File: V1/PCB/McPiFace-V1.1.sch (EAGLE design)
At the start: 10 parts, among them J1 MC_PI_FACE_CONNECTORS_LEDSSIDE

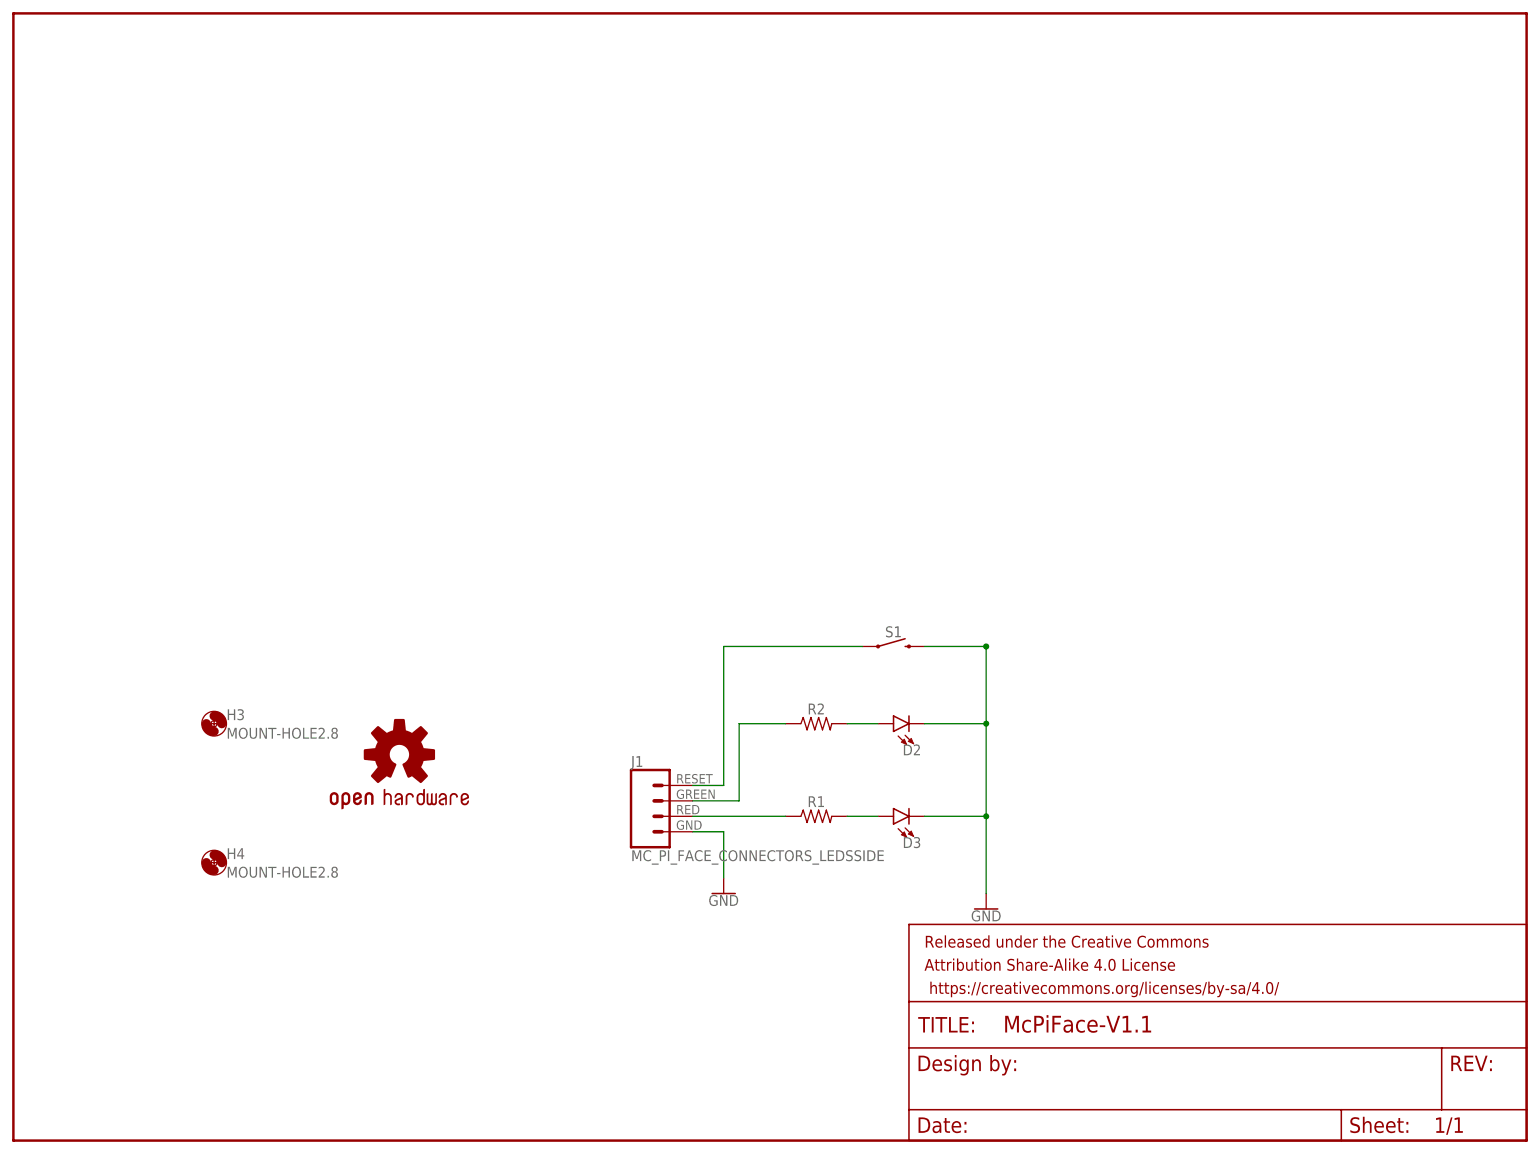
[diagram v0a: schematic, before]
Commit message: Adding V1.1 PCB.
Uses common layout for LEDs, removed vent hole.
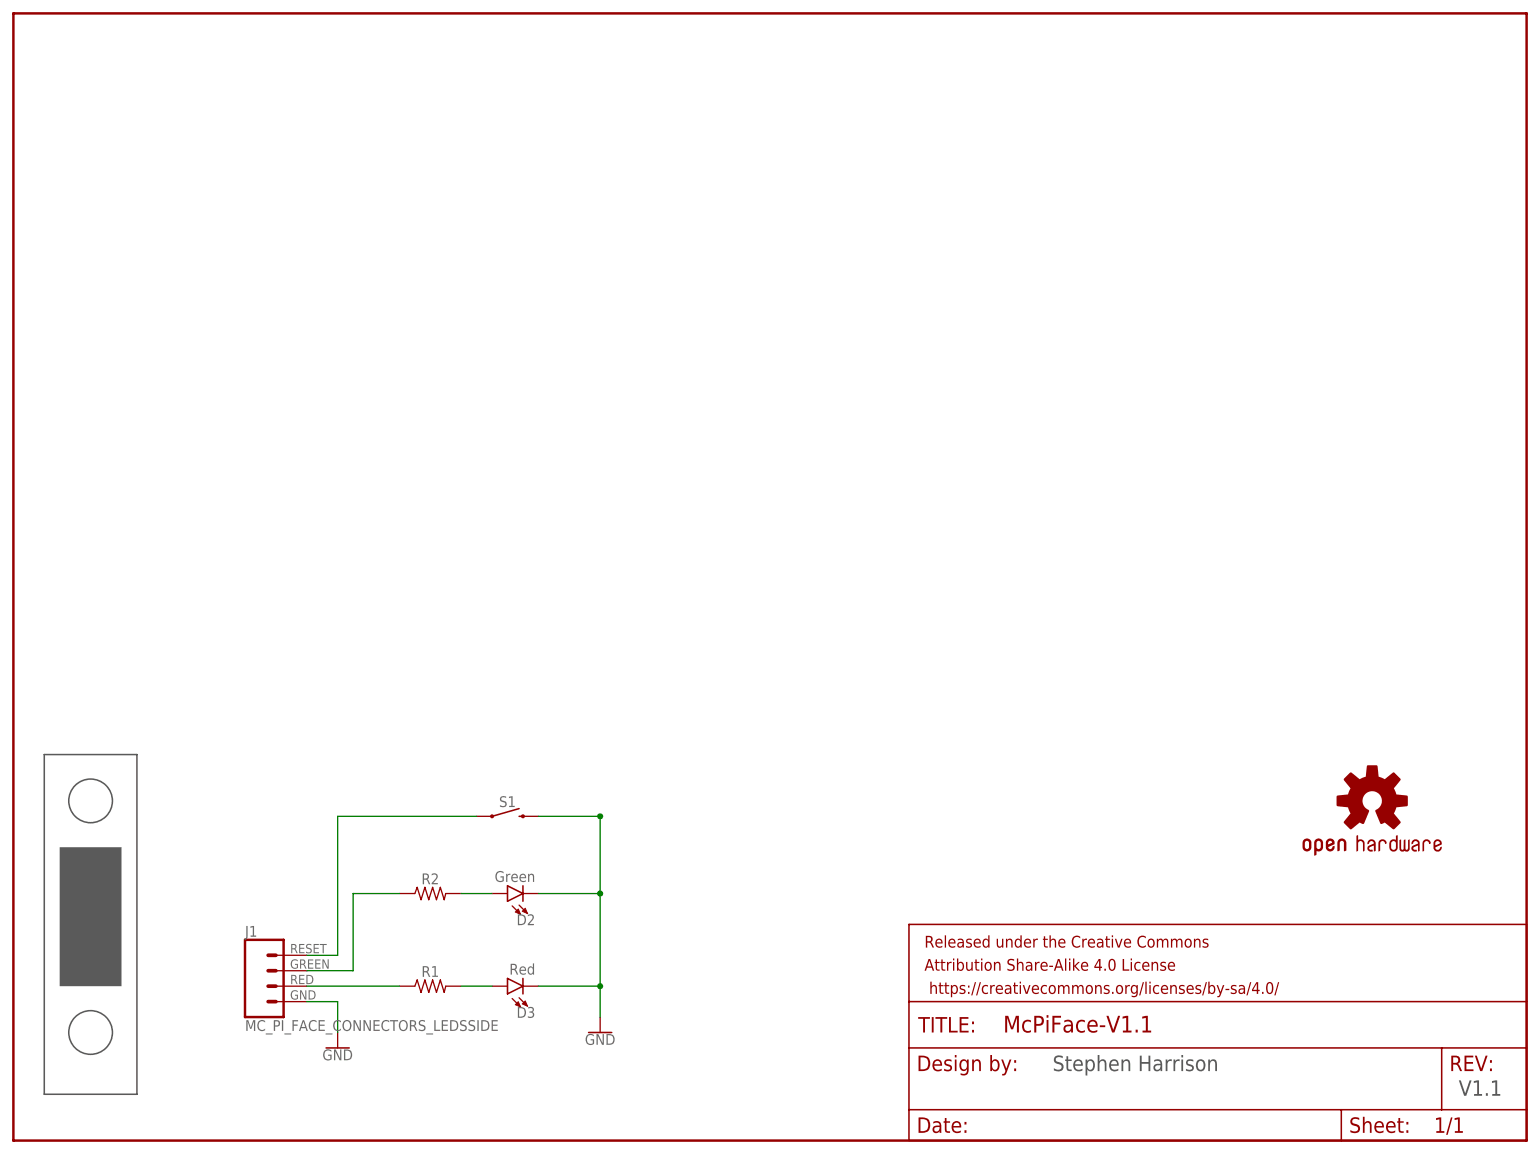
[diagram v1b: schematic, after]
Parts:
- removed H3, H4: MOUNT-HOLE2.8, holes:MOUNT-HOLE2.8
- added U$1: MC_PI_FACE_PANELSINGLE, McPiFace:MC_PI_FACE_PANELSINGLE
- D2: value (none) -> Green
- D3: value (none) -> Red
- R1, R2: device SparkFun-Resistors:RESISTOR1206 -> SparkFun-Resistors:RESISTOR0805
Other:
- note added: "Stephen Harrison"
- note added: "V1.1"
- moved on the sheet: D2, D3, J1, R1, R2, S1
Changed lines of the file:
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@@
 <parts>
 <part name="LOGO1" library="SparkFun-Aesthetics" deviceset="OSHW-LOGO" device="L"/>
-<part name="H3" library="holes" deviceset="MOUNT-HOLE" device="2.8"/>
-<part name="H4" library="holes" deviceset="MOUNT-HOLE" device="2.8"/>
-<part name="D2" library="ThingySticks" deviceset="LED" device="LED-1206-BOTTOM-2.0MM-GREEN"/>
-<part name="D3" library="ThingySticks" deviceset="LED" device="LED-1206-BOTTOM-2.0MM-RED"/>
-<part name="R1" library="SparkFun-Resistors" deviceset="RESISTOR" device="1206" value=" "/>
-<part name="R2" library="SparkFun-Resistors" deviceset="RESISTOR" device="1206" value=" "/>
+<part name="D2" library="ThingySticks" deviceset="LED" device="LED-1206-BOTTOM-2.0MM-GREEN" value="Green"/>
+<part name="D3" library="ThingySticks" deviceset="LED" device="LED-1206-BOTTOM-2.0MM-RED" value="Red"/>
+<part name="R1" library="SparkFun-Resistors" deviceset="RESISTOR" device="0805" value=" "/>
+<part name="R2" library="SparkFun-Resistors" deviceset="RESISTOR" device="0805" value=" "/>
 <part name="GND1" library="SparkFun-PowerSymbols" deviceset="GND" device=""/>
 <part name="J1" library="McPiFace" deviceset="MC_PI_FACE_CONNECTORS_LEDS" device="SIDE"/>
@@
 <part name="FRAME1" library="SparkFun-Aesthetics" deviceset="FRAME-LETTER" device=""/>
 <part name="S1" library="ThingySticks" deviceset="MOMENTARY-SWITCH-SPST" device="TACKTILE_SWITCH_PTH_6.0MM_NO_TOP_RESIST"/>
+<part name="U$1" library="McPiFace" deviceset="MC_PI_FACE_PANEL" device="SINGLE"/>
 </parts>
 <sheets>
 <sheet>
 <plain>
+<text x="170.942" y="11.43" size="2.54" layer="97">Stephen Harrison</text>
+<text x="237.744" y="7.366" size="2.54" layer="97">V1.1</text>
 </plain>
 <instances>
-<instance part="LOGO1" gate="G$1" x="63.5" y="63.5"/>
-<instance part="H3" gate="G$1" x="33.02" y="68.58"/>
-<instance part="H4" gate="G$1" x="33.02" y="45.72"/>
-<instance part="D2" gate="G$1" x="144.78" y="68.58" rot="R90"/>
-<instance part="D3" gate="G$1" x="144.78" y="53.34" rot="R90"/>
-<instance part="R1" gate="G$1" x="132.08" y="53.34"/>
-<instance part="R2" gate="G$1" x="132.08" y="68.58"/>
-<instance part="GND1" gate="1" x="160.02" y="38.1"/>
-<instance part="J1" gate="G$1" x="106.68" y="53.34"/>
-<instance part="GND2" gate="1" x="116.84" y="40.64"/>
+<instance part="LOGO1" gate="G$1" x="223.52" y="55.88"/>
+<instance part="D2" gate="G$1" x="81.28" y="40.64" rot="R90"/>
+<instance part="D3" gate="G$1" x="81.28" y="25.4" rot="R90"/>
+<instance part="R1" gate="G$1" x="68.58" y="25.4"/>
+<instance part="R2" gate="G$1" x="68.58" y="40.64"/>
+<instance part="GND1" gate="1" x="96.52" y="17.78"/>
+<instance part="J1" gate="G$1" x="43.18" y="25.4"/>
+<instance part="GND2" gate="1" x="53.34" y="15.24"/>
 <instance part="FRAME1" gate="G$1" x="0" y="0"/>
 <instance part="FRAME1" gate="V" x="147.32" y="0"/>
-<instance part="S1" gate="G$1" x="144.78" y="81.28" smashed="yes">
-<attribute name="NAME" x="144.78" y="82.804" size="1.778" layer="95" font="vector" align="bottom-center"/>
+<instance part="S1" gate="G$1" x="81.28" y="53.34" smashed="yes">
+<attribute name="NAME" x="81.28" y="54.864" size="1.778" layer="95" font="vector" align="bottom-center"/>
 </instance>
+<instance part="U$1" gate="G$1" x="5.08" y="7.62"/>
 </instances>
 <busses>
@@
 <pinref part="D2" gate="G$1" pin="A"/>
 <pinref part="R2" gate="G$1" pin="2"/>
-<wire x1="137.16" y1="68.58" x2="142.24" y2="68.58" width="0.1524" layer="91"/>
+<wire x1="73.66" y1="40.64" x2="78.74" y2="40.64" width="0.1524" layer="91"/>
 </segment>
 </net>
@@
 <pinref part="D3" gate="G$1" pin="A"/>
 <pinref part="R1" gate="G$1" pin="2"/>
-<wire x1="137.16" y1="53.34" x2="142.24" y2="53.34" width="0.1524" layer="91"/>
+<wire x1="73.66" y1="25.4" x2="78.74" y2="25.4" width="0.1524" layer="91"/>
 </segment>
 </net>
@@
 <pinref part="R1" gate="G$1" pin="1"/>
 <pinref part="J1" gate="G$1" pin="RED"/>
-<wire x1="111.76" y1="53.34" x2="127" y2="53.34" width="0.1524" layer="91"/>
+<wire x1="48.26" y1="25.4" x2="63.5" y2="25.4" width="0.1524" layer="91"/>
 </segment>
 </net>
@@
 <segment>
 <pinref part="R2" gate="G$1" pin="1"/>
-<wire x1="127" y1="68.58" x2="119.38" y2="68.58" width="0.1524" layer="91"/>
+<wire x1="63.5" y1="40.64" x2="55.88" y2="40.64" width="0.1524" layer="91"/>
 <pinref part="J1" gate="G$1" pin="GREEN"/>
-<wire x1="111.76" y1="55.88" x2="119.38" y2="55.88" width="0.1524" layer="91"/>
-<wire x1="119.38" y1="55.88" x2="119.38" y2="68.58" width="0.1524" layer="91"/>
+<wire x1="48.26" y1="27.94" x2="55.88" y2="27.94" width="0.1524" layer="91"/>
+<wire x1="55.88" y1="27.94" x2="55.88" y2="40.64" width="0.1524" layer="91"/>
 </segment>
 </net>
@@
 <segment>
 <pinref part="J1" gate="G$1" pin="RESET"/>
-<wire x1="111.76" y1="58.42" x2="116.84" y2="58.42" width="0.1524" layer="91"/>
-<wire x1="116.84" y1="58.42" x2="116.84" y2="81.28" width="0.1524" layer="91"/>
+<wire x1="48.26" y1="30.48" x2="53.34" y2="30.48" width="0.1524" layer="91"/>
+<wire x1="53.34" y1="30.48" x2="53.34" y2="53.34" width="0.1524" layer="91"/>
 <pinref part="S1" gate="G$1" pin="1"/>
-<wire x1="116.84" y1="81.28" x2="139.7" y2="81.28" width="0.1524" layer="91"/>
+<wire x1="53.34" y1="53.34" x2="76.2" y2="53.34" width="0.1524" layer="91"/>
 </segment>
 </net>
 <net name="GND" class="0">
 <segment>
-<wire x1="149.86" y1="81.28" x2="160.02" y2="81.28" width="0.1524" layer="91"/>
-<wire x1="160.02" y1="81.28" x2="160.02" y2="68.58" width="0.1524" layer="91"/>
+<wire x1="86.36" y1="53.34" x2="96.52" y2="53.34" width="0.1524" layer="91"/>
+<wire x1="96.52" y1="53.34" x2="96.52" y2="40.64" width="0.1524" layer="91"/>
 <pinref part="D3" gate="G$1" pin="C"/>
-<wire x1="160.02" y1="68.58" x2="160.02" y2="53.34" width="0.1524" layer="91"/>
-<wire x1="160.02" y1="53.34" x2="160.02" y2="40.64" width="0.1524" layer="91"/>
-<wire x1="149.86" y1="53.34" x2="160.02" y2="53.34" width="0.1524" layer="91"/>
-<wire x1="149.86" y1="68.58" x2="160.02" y2="68.58" width="0.1524" layer="91"/>
+<wire x1="96.52" y1="40.64" x2="96.52" y2="25.4" width="0.1524" layer="91"/>
+<wire x1="96.52" y1="25.4" x2="96.52" y2="20.32" width="0.1524" layer="91"/>
+<wire x1="86.36" y1="25.4" x2="96.52" y2="25.4" width="0.1524" layer="91"/>
+<wire x1="86.36" y1="40.64" x2="96.52" y2="40.64" width="0.1524" layer="91"/>
 <pinref part="D2" gate="G$1" pin="C"/>
 <pinref part="GND1" gate="1" pin="GND"/>
-<junction x="160.02" y="53.34"/>
-<junction x="160.02" y="68.58"/>
-<junction x="160.02" y="81.28"/>
+<junction x="96.52" y="25.4"/>
+<junction x="96.52" y="40.64"/>
+<junction x="96.52" y="53.34"/>
 <pinref part="S1" gate="G$1" pin="2"/>
 </segment>
 <segment>
 <pinref part="J1" gate="G$1" pin="GND"/>
-<wire x1="111.76" y1="50.8" x2="116.84" y2="50.8" width="0.1524" layer="91"/>
-<wire x1="116.84" y1="50.8" x2="116.84" y2="43.18" width="0.1524" layer="91"/>
+<wire x1="48.26" y1="22.86" x2="53.34" y2="22.86" width="0.1524" layer="91"/>
+<wire x1="53.34" y1="22.86" x2="53.34" y2="17.78" width="0.1524" layer="91"/>
 <pinref part="GND2" gate="1" pin="GND"/>
 </segment>
